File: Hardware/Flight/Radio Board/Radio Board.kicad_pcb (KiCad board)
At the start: 2 copper layers, 82 x 82 mm, 24 parts, among them J1 Bus_Connector, J2 Conn_Coaxial, J3 Conn_Coaxial, U1 RFM95W-915S2, U2 RFM95W-915S2

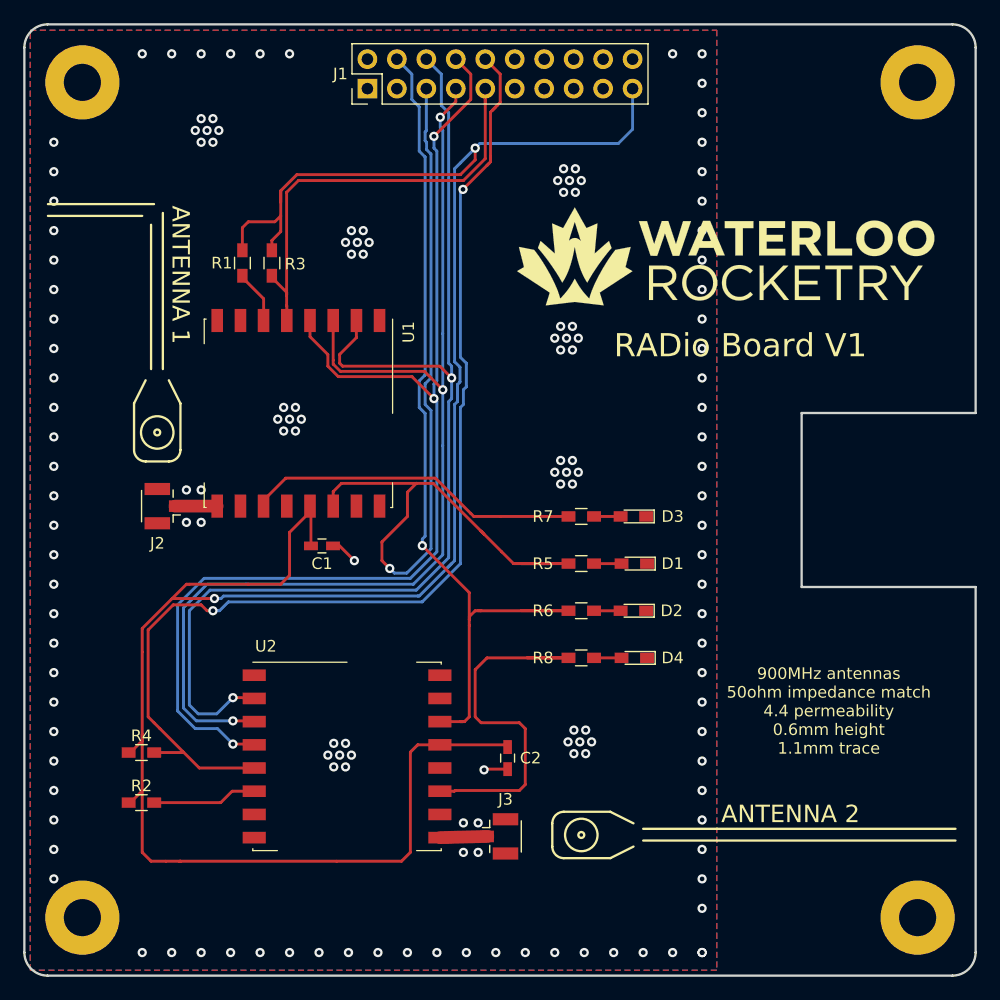
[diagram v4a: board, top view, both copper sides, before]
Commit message: Radio board review fixes Spaced resistors away from LEDs Adjusted antenna trace Set solder mask clearance to 0
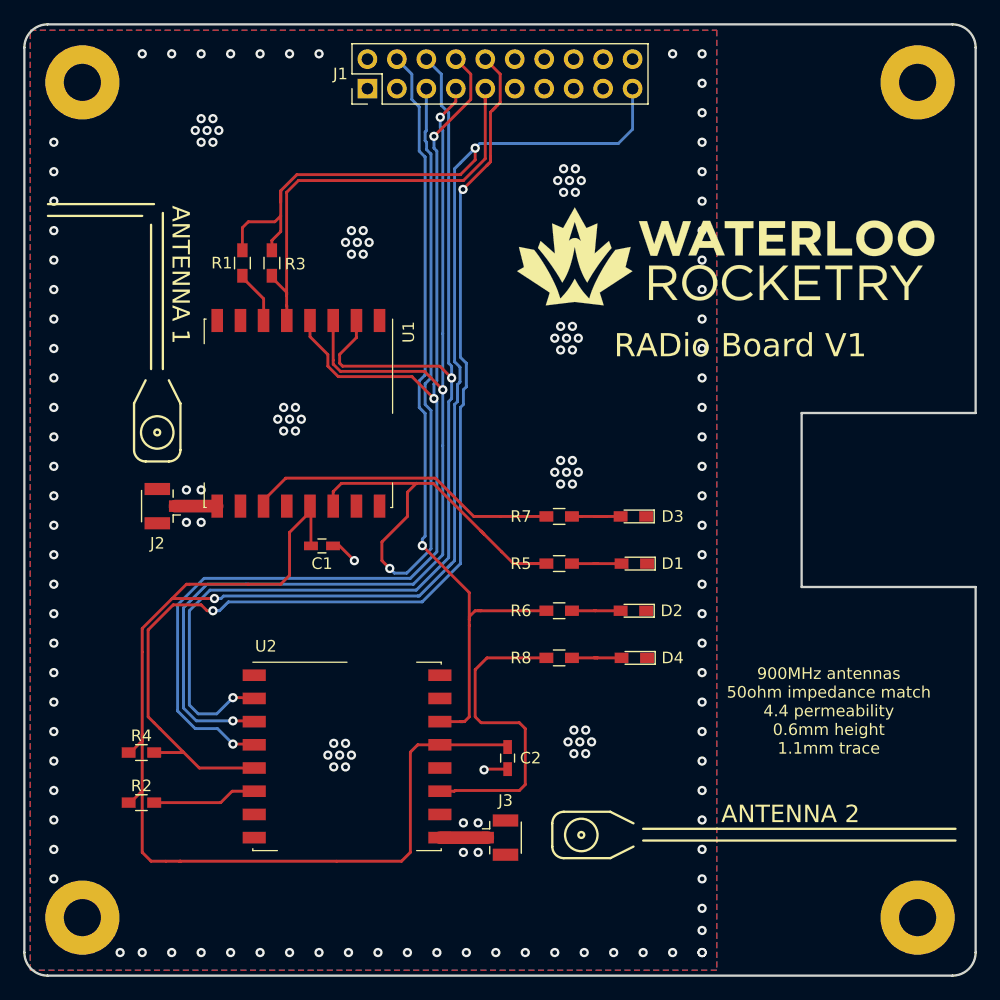
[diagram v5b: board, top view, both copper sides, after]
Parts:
- moved R5 1.91 mm to (46.1, 46.5)
- moved R6 1.91 mm to (46.1, 50.5)
- moved R7 1.91 mm to (46.1, 42.4)
- moved R8 1.91 mm to (46.1, 54.6)
- moved J3 0.10 mm to (41.0, 70.1)
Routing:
- net /INT2: track 76.2 -> 70.2 mm
- net /INT1: track 86.2 -> 80.4 mm
- net Net-(R8-Pad2): track 33.3 -> 27.8 mm
- net Net-(D3-Pad2): track 2.29 -> 5.25 mm
- net Net-(D4-Pad2): track 2.37 -> 4.57 mm
- net Net-(D1-Pad2): track 2.37 -> 4.57 mm
- net Net-(D2-Pad2): track 2.29 -> 4.36 mm
- net Net-(R7-Pad2): track 28.9 -> 27.0 mm
- net GND: vias 150 -> 153
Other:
- rule pad_to_mask_clearance: 0.2 -> 0
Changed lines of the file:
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@@
     (thickness 1.6)
     (drawings 41)
-    (tracks 451)
+    (tracks 458)
     (zones 0)
     (modules 24)
@@
     (pad_size 1.524 1.524)
     (pad_drill 0.762)
-    (pad_to_mask_clearance 0.2)
+    (pad_to_mask_clearance 0)
     (aux_axis_origin 0 0)
     (visible_elements 7FFFFFFF)
     (pcbplotparams
-      (layerselection 0x010fc_ffffffff)
+      (layerselection 0x010f0_ffffffff)
       (usegerberextensions false)
       (usegerberattributes false)
@@
       (outputformat 1)
       (mirror false)
-      (drillshape 1)
+      (drillshape 0)
       (scaleselection 1)
-      (outputdirectory ""))
+      (outputdirectory "Gerbers/"))
   )
   (net 0 "")
@@
   )
   (module "Downloaded Connectors:U.FL_Hirose_U.FL-R-SMT-1_Vertical" (layer F.Cu)
-    (at 41 70)
+    (at 41 70.104)
     (descr "Hirose U.FL Coaxial https://www.hirose.com/product/en/products/U.FL/U.FL-R-SMT-1%2810%29/")
     (tags "Hirose U.FL Coaxial")
@@
   )
   (module Resistors_SMD:R_0603_HandSoldering (layer F.Cu)
-    (at 48.006 46.482 180)
+    (at 46.101 46.482 180)
     (descr "Resistor SMD 0603, hand soldering")
     (tags "resistor 0603")
@@
   )
   (module Resistors_SMD:R_0603_HandSoldering (layer F.Cu)
-    (at 48.006 50.546 180)
+    (at 46.101 50.546 180)
     (descr "Resistor SMD 0603, hand soldering")
     (tags "resistor 0603")
@@
   )
   (module Resistors_SMD:R_0603_HandSoldering (layer F.Cu)
-    (at 48.006 42.418 180)
+    (at 46.101 42.418 180)
     (descr "Resistor SMD 0603, hand soldering")
     (tags "resistor 0603")
@@
   )
   (module Resistors_SMD:R_0603_HandSoldering (layer F.Cu)
-    (at 48.006 54.61 180)
+    (at 46.101 54.61 180)
     (descr "Resistor SMD 0603, hand soldering")
     (tags "resistor 0603")
@@
   (via (at 47.244 28.067) (size 0.8) (drill 0.4) (layers F.Cu B.Cu) (net 1))
   (via (at 47.244 26.035) (size 0.8) (drill 0.4) (layers F.Cu B.Cu) (net 1))
+  (via (at 25.4 2.54) (size 0.8) (drill 0.4) (layers F.Cu B.Cu) (net 1))
+  (via (at 58.42 78.105) (size 0.8) (drill 0.4) (layers F.Cu B.Cu) (net 1))
+  (via (at 8.255 80.01) (size 0.8) (drill 0.4) (layers F.Cu B.Cu) (net 1))
   (segment (start 13.339559 72.136) (end 13.462 72.136) (width 0.25) (layer F.Cu) (net 2))
   (segment (start 13.462 72.136) (end 26.924 72.136) (width 0.25) (layer F.Cu) (net 2))
@@
   (segment (start 12.988 41.529) (end 16.621 41.529) (width 1.1) (layer F.Cu) (net 10))
   (segment (start 39.911515 70.038485) (end 39.95 70) (width 0.25) (layer F.Cu) (net 11))
-  (segment (start 39.95 70) (end 35.814 70.104) (width 1.1) (layer F.Cu) (net 11))
+  (segment (start 35.814 70.104) (end 39.95 70.104) (width 1.1) (layer F.Cu) (net 11))
   (segment (start 18.796 21.824) (end 18.796 21.674) (width 0.25) (layer F.Cu) (net 24))
   (segment (start 20.622 23.65) (end 18.796 21.824) (width 0.25) (layer F.Cu) (net 24))
@@
   (segment (start 17.913529 66.104) (end 16.930044 67.087485) (width 0.25) (layer F.Cu) (net 25))
   (segment (start 19.814 66.104) (end 17.913529 66.104) (width 0.25) (layer F.Cu) (net 25))
-  (segment (start 49.106 46.482) (end 51.478 46.482) (width 0.25) (layer F.Cu) (net 26))
-  (segment (start 49.106 50.546) (end 51.394 50.546) (width 0.25) (layer F.Cu) (net 27))
-  (segment (start 49.106 42.418) (end 51.394 42.418) (width 0.25) (layer F.Cu) (net 28))
-  (segment (start 49.106 54.61) (end 51.478 54.61) (width 0.25) (layer F.Cu) (net 29))
+  (segment (start 47.201 46.482) (end 49.403 46.482) (width 0.25) (layer F.Cu) (net 26))
+  (segment (start 49.106 46.482) (end 49.403 46.482) (width 0.25) (layer F.Cu) (net 26))
+  (segment (start 49.403 46.482) (end 51.478 46.482) (width 0.25) (layer F.Cu) (net 26))
+  (segment (start 49.276 50.546) (end 47.201 50.546) (width 0.25) (layer F.Cu) (net 27))
+  (segment (start 49.276 50.546) (end 51.394 50.546) (width 0.25) (layer F.Cu) (net 27))
+  (segment (start 49.106 50.546) (end 49.276 50.546) (width 0.25) (layer F.Cu) (net 27))
+  (segment (start 48.051 42.418) (end 50.165 42.418) (width 0.25) (layer F.Cu) (net 28))
+  (segment (start 47.201 42.418) (end 48.051 42.418) (width 0.25) (layer F.Cu) (net 28))
+  (segment (start 49.106 42.418) (end 50.165 42.418) (width 0.25) (layer F.Cu) (net 28))
+  (segment (start 50.165 42.418) (end 51.394 42.418) (width 0.25) (layer F.Cu) (net 28))
+  (segment (start 49.403 54.61) (end 47.201 54.61) (width 0.25) (layer F.Cu) (net 29))
+  (segment (start 49.403 54.61) (end 51.478 54.61) (width 0.25) (layer F.Cu) (net 29))
+  (segment (start 49.106 54.61) (end 49.403 54.61) (width 0.25) (layer F.Cu) (net 29))
   (segment (start 40.767 6.985) (end 40.64 7.112) (width 0.25) (layer F.Cu) (net 30))
   (segment (start 41.021 6.731) (end 40.767 6.985) (width 0.25) (layer F.Cu) (net 30))
@@
   (segment (start 36.83 30.48) (end 36.83 29.464) (width 0.25) (layer B.Cu) (net 34))
   (segment (start 36.83 29.464) (end 36.576 29.21) (width 0.25) (layer B.Cu) (net 34))
-  (segment (start 46.906 46.482) (end 42.814 46.482) (width 0.25) (layer F.Cu) (net 35))
   (segment (start 35.24801 39.56601) (end 39.37 43.688) (width 0.25) (layer F.Cu) (net 35))
   (segment (start 39.37 43.688) (end 39.624 43.942) (width 0.25) (layer F.Cu) (net 35))
@@
   (segment (start 41.148 45.466) (end 39.37 43.688) (width 0.25) (layer F.Cu) (net 35))
   (segment (start 45.212 46.482) (end 42.418 46.482) (width 0.25) (layer F.Cu) (net 35))
-  (segment (start 46.906 46.482) (end 45.212 46.482) (width 0.25) (layer F.Cu) (net 35))
   (segment (start 32.962001 47.301999) (end 31.895999 47.301999) (width 0.25) (layer B.Cu) (net 35))
   (segment (start 35.052 45.212) (end 32.962001 47.301999) (width 0.25) (layer B.Cu) (net 35))
@@
   (segment (start 34.544 10.033) (end 34.671 10.16) (width 0.25) (layer B.Cu) (net 35))
   (segment (start 34.671 10.795) (end 35.052 11.176) (width 0.25) (layer B.Cu) (net 35))
-  (segment (start 42.814 50.546) (end 46.906 50.546) (width 0.25) (layer F.Cu) (net 36))
   (segment (start 38.354 51.054) (end 38.862 50.546) (width 0.25) (layer F.Cu) (net 36))
   (segment (start 38.354 51.308) (end 38.354 51.054) (width 0.25) (layer F.Cu) (net 36))
   (segment (start 39.37 50.546) (end 38.862 50.546) (width 0.25) (layer F.Cu) (net 36))
   (segment (start 39.37 50.546) (end 39.116 50.546) (width 0.25) (layer F.Cu) (net 36))
-  (segment (start 46.906 50.546) (end 39.37 50.546) (width 0.25) (layer F.Cu) (net 36))
   (segment (start 33.401 6.477) (end 33.401 4.291) (width 0.25) (layer B.Cu) (net 36))
   (segment (start 33.401 4.291) (end 32.11 3) (width 0.25) (layer B.Cu) (net 36))
@@
   (segment (start 34.544 11.43) (end 34.036 10.922) (width 0.25) (layer B.Cu) (net 36))
   (segment (start 34.036 30.734) (end 34.544 30.226) (width 0.25) (layer B.Cu) (net 36))
+  (segment (start 39.37 50.546) (end 45.001 50.546) (width 0.25) (layer F.Cu) (net 36))
+  (segment (start 41.01959 42.418) (end 45.001 42.418) (width 0.25) (layer F.Cu) (net 37))
+  (segment (start 38.73641 42.418) (end 41.01959 42.418) (width 0.25) (layer F.Cu) (net 37))
+  (segment (start 35.434411 39.116001) (end 38.73641 42.418) (width 0.25) (layer F.Cu) (net 37))
   (segment (start 22.534 39.116) (end 35.434411 39.116001) (width 0.25) (layer F.Cu) (net 37))
+  (segment (start 20.622 41.528) (end 20.622 41.028) (width 0.25) (layer F.Cu) (net 37))
   (segment (start 20.622 41.028) (end 22.534 39.116) (width 0.25) (layer F.Cu) (net 37))
-  (segment (start 20.622 41.528) (end 20.622 41.028) (width 0.25) (layer F.Cu) (net 37))
-  (segment (start 41.01959 42.418) (end 46.906 42.418) (width 0.25) (layer F.Cu) (net 37))
-  (segment (start 38.73641 42.418) (end 38.48241 42.164) (width 0.25) (layer F.Cu) (net 37))
-  (segment (start 41.01959 42.418) (end 38.73641 42.418) (width 0.25) (layer F.Cu) (net 37))
-  (segment (start 35.434411 39.116001) (end 38.48241 42.164) (width 0.25) (layer F.Cu) (net 37))
-  (segment (start 43.322 54.61) (end 46.906 54.61) (width 0.25) (layer F.Cu) (net 38))
   (segment (start 39.37 60.198) (end 38.862 59.69) (width 0.25) (layer F.Cu) (net 38))
   (segment (start 42.672 60.198) (end 39.37 60.198) (width 0.25) (layer F.Cu) (net 38))
@@
   (segment (start 43.18 60.706) (end 42.672 60.198) (width 0.25) (layer F.Cu) (net 38))
   (segment (start 39.878 54.61) (end 38.862 55.626) (width 0.25) (layer F.Cu) (net 38))
-  (segment (start 46.906 54.61) (end 39.878 54.61) (width 0.25) (layer F.Cu) (net 38))
   (segment (start 38.862 59.69) (end 38.862 55.626) (width 0.25) (layer F.Cu) (net 38))
+  (segment (start 39.878 54.61) (end 45.001 54.61) (width 0.25) (layer F.Cu) (net 38))
   (zone (net 1) (net_name GND) (layer F.Cu) (hatch edge 0.508)
     (connect_pads (clearance 0.508))
